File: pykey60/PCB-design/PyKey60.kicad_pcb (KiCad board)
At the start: 2 copper layers, 285 x 95 mm, 227 parts, among them J1 USB_C_Receptacle_USB2.0, J2 Conn_01x03, J3 Conn_01x04, J4 Conn_01x06, SW1 SW_SPST, SW2 SW_SPDT, U1 CherryMX_LTST-A683CEGBW, U10 CherryMX_LTST-A683CEGBW, U11 CherryMX_LTST-A683CEGBW, U12 CherryMX_LTST-A683CEGBW, U13 CherryMX_LTST-A683CEGBW, U14 CherryMX_LTST-A683CEGBW, U15 CherryMX_LTST-A683CEGBW, U16 CherryMX_LTST-A683CEGBW, U17 CherryMX_LTST-A683CEGBW, U18 CherryMX_LTST-A683CEGBW, U19 CherryMX_LTST-A683CEGBW, U2 CherryMX_LTST-A683CEGBW, U20 CherryMX_LTST-A683CEGBW, U21 CherryMX_LTST-A683CEGBW, U22 CherryMX_LTST-A683CEGBW, U23 CherryMX_LTST-A683CEGBW, U24 CherryMX_LTST-A683CEGBW, U25 CherryMX_LTST-A683CEGBW, U26 CherryMX_LTST-A683CEGBW, U27 CherryMX_LTST-A683CEGBW, U28 CherryMX_LTST-A683CEGBW, U29 CherryMX_LTST-A683CEGBW, U3 CherryMX_LTST-A683CEGBW, U30 CherryMX_LTST-A683CEGBW, U31 CherryMX_LTST-A683CEGBW, U32 CherryMX_LTST-A683CEGBW, U33 CherryMX_LTST-A683CEGBW, U34 CherryMX_LTST-A683CEGBW, U35 CherryMX_LTST-A683CEGBW, U36 CherryMX_LTST-A683CEGBW, U37 CherryMX_LTST-A683CEGBW, U38 CherryMX_LTST-A683CEGBW, U39 CherryMX_LTST-A683CEGBW, U4 CherryMX_LTST-A683CEGBW, U40 CherryMX_LTST-A683CEGBW, U41 CherryMX_LTST-A683CEGBW, U42 CherryMX_LTST-A683CEGBW, U43 CherryMX_LTST-A683CEGBW, U44 CherryMX_LTST-A683CEGBW, U45 CherryMX_LTST-A683CEGBW, U46 CherryMX_LTST-A683CEGBW, U47 CherryMX_LTST-A683CEGBW, U48 CherryMX_LTST-A683CEGBW, U49 CherryMX_LTST-A683CEGBW, U5 CherryMX_LTST-A683CEGBW, U50 CherryMX_LTST-A683CEGBW, U51 CherryMX_LTST-A683CEGBW, U52 CherryMX_LTST-A683CEGBW, U53 CherryMX_LTST-A683CEGBW, U54 CherryMX_LTST-A683CEGBW, U55 CherryMX_LTST-A683CEGBW, U56 CherryMX_LTST-A683CEGBW, U57 CherryMX_LTST-A683CEGBW, U58 CherryMX_LTST-A683CEGBW, U59 CherryMX_LTST-A683CEGBW, U6 CherryMX_LTST-A683CEGBW, U60 CherryMX_LTST-A683CEGBW, U61 CherryMX_LTST-A683CEGBW, U62 RP2040, U63 USBLC6-2SC6, U64 W25Q128JVS, U65 AMS1117-3.3, U7 CherryMX_LTST-A683CEGBW, U8 CherryMX_LTST-A683CEGBW, U9 CherryMX_LTST-A683CEGBW, Y1 12MHz

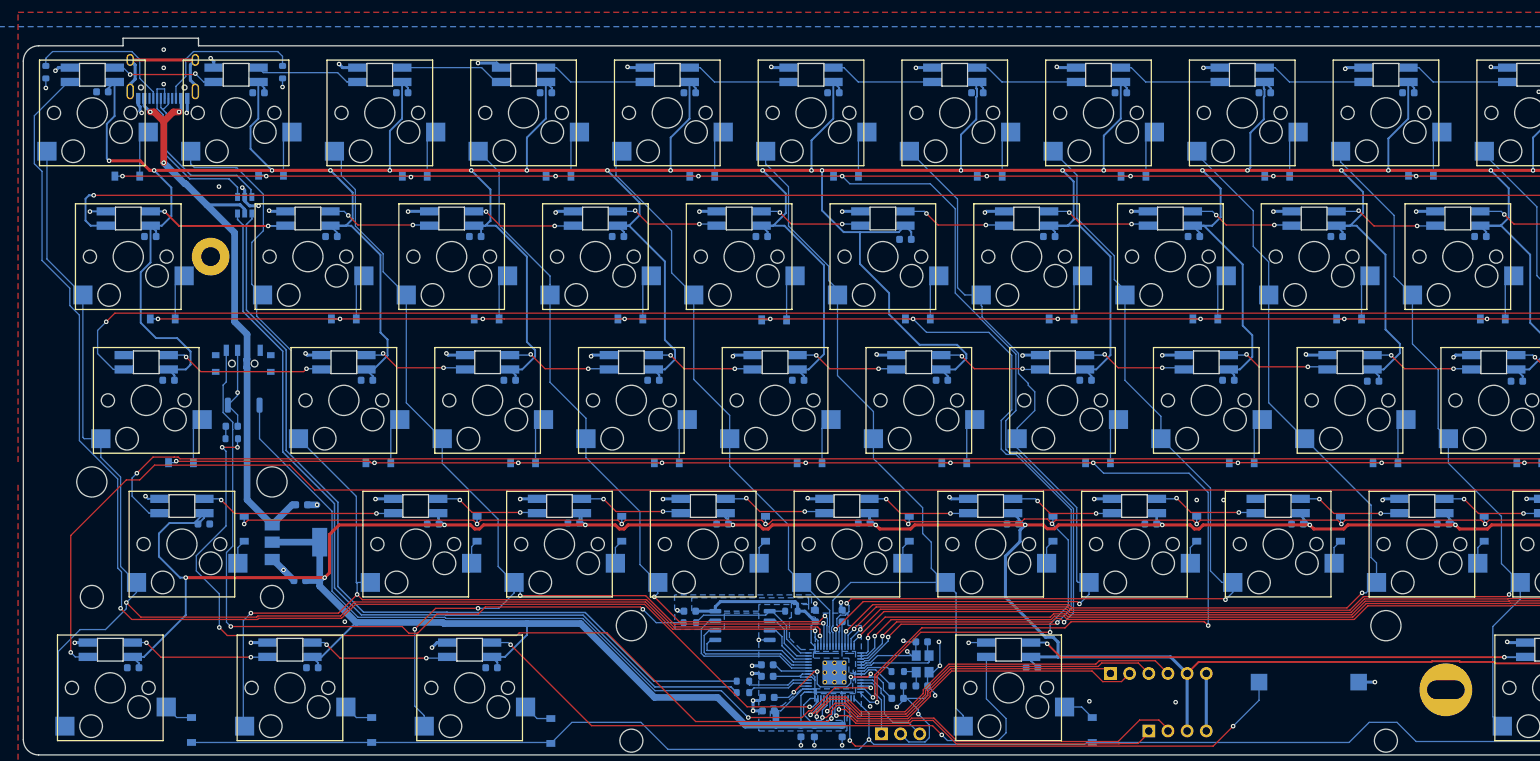
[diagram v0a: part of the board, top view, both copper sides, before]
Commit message: re-org and added folder for pykey87 (TKL!)
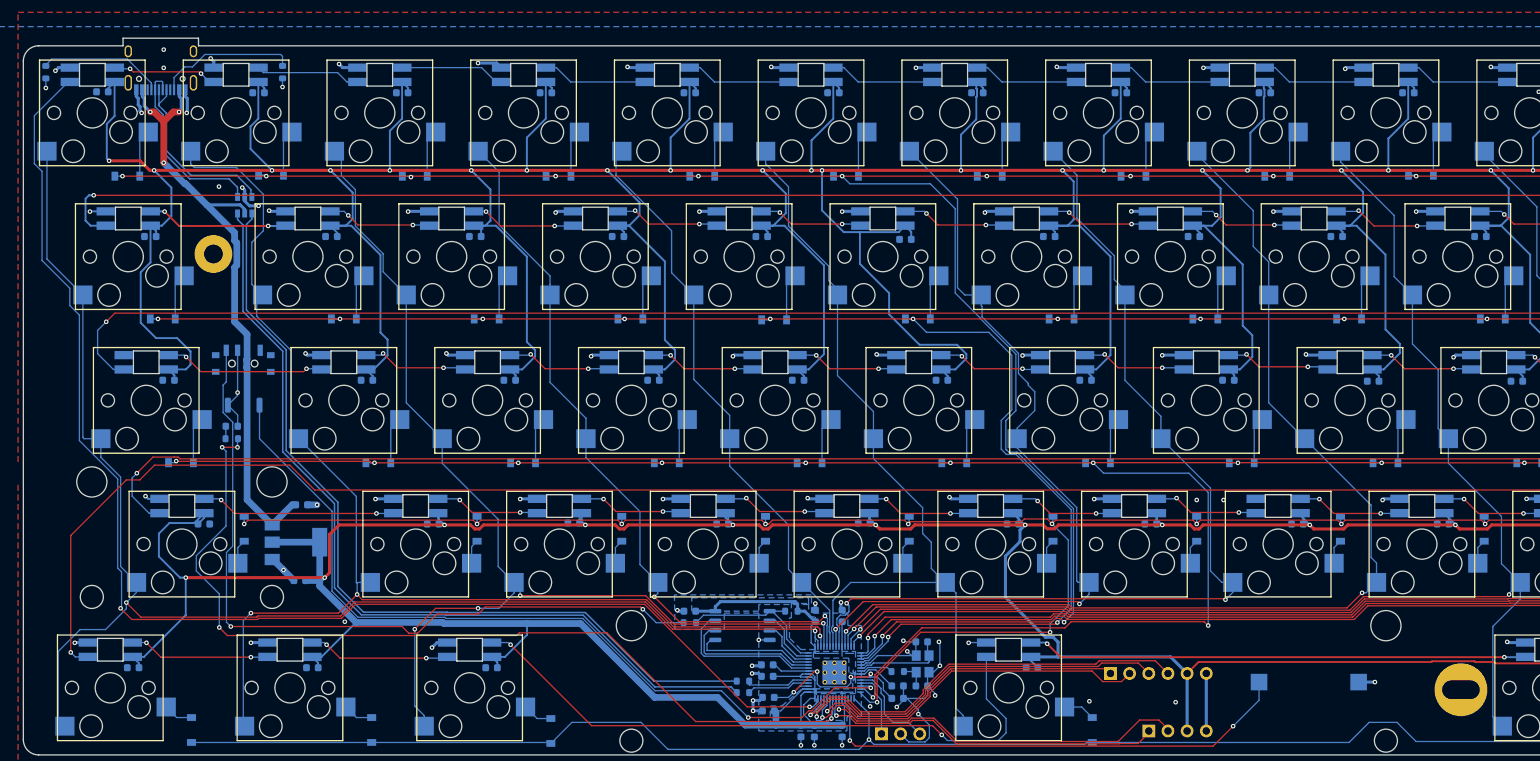
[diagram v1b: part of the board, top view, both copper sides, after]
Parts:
- moved J1 1.17 mm to (80.5, 66.7)
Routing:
- net Net-(J1-PadS1): track 18.1 -> 0.00 mm
- net Net-(J1-PadA5): track 20.2 -> 16.6 mm
- net VBUS: track 78.5 -> 81.2 mm
- net GND: track 236.3 -> 238.8 mm, vias 100 -> 99
- net /USB+: track 23.4 -> 25.4 mm
- net Net-(J1-PadB5): track 20.5 -> 18.6 mm
- net Net-(U1-Pad5): track 14.0 -> 15.1 mm
- net /USB-: track 24.0 -> 24.9 mm
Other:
- board text added: "CERN-OHL-W 2021-09-29 - Pierre Constantineau"
- board text removed: "CERN-OHL-W 2021-09-01 - Pierre Constantineau"
